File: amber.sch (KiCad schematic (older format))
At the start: 41 parts, among them J1 MJ-4PP-9

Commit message: Use a mid-mount TRRS jack SJ 43504
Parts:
- removed J1: MJ-4PP-9, kbd:MJ-4PP-9, symbol kbd:MJ-4PP-9
- added J?: SJ-43504-SMT-TR, amber:CUI_SJ-43504-SMT-TR-dual, symbol SJ-43504-SMT-TR:SJ-43504-SMT-TR
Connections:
- no-connect marks 5 -> 7
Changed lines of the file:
@@
 	8000 2100 8000 1800
-$Comp
-L kbd:MJ-4PP-9 J1
-U 1 1 60243402
-P 9400 4575
-F 0 "J1" H 9431 4851 50  0000 C CNN
-F 1 "MJ-4PP-9" H 9431 4760 50  0000 C CNN
-F 2 "kbd:MJ-4PP-9" H 9675 4750 50  0001 C CNN
-F 3 "~" H 9675 4750 50  0001 C CNN
-	1    9400 4575
-	1    0    0    -1
-$EndComp
 $Comp
 L power:GND #PWR05
 U 1 1 60243D5F
-P 9825 4725
-F 0 "#PWR05" H 9825 4475 50  0001 C CNN
-F 1 "GND" H 9830 4552 50  0000 C CNN
-F 2 "" H 9825 4725 50  0001 C CNN
-F 3 "" H 9825 4725 50  0001 C CNN
-	1    9825 4725
+P 9250 4675
+F 0 "#PWR05" H 9250 4425 50  0001 C CNN
+F 1 "GND" H 9255 4502 50  0000 C CNN
+F 2 "" H 9250 4675 50  0001 C CNN
+F 3 "" H 9250 4675 50  0001 C CNN
+	1    9250 4675
 	1    0    0    -1
 $EndComp
 Wire Wire Line
-	9600 4600 9825 4600
+	9025 4550 9250 4550
 Wire Wire Line
-	9825 4600 9825 4725
+	9250 4550 9250 4675
 $Comp
 L power:VCC #PWR04
 U 1 1 60246E67
-P 9825 4400
-F 0 "#PWR04" H 9825 4250 50  0001 C CNN
-F 1 "VCC" H 9840 4573 50  0000 C CNN
-F 2 "" H 9825 4400 50  0001 C CNN
-F 3 "" H 9825 4400 50  0001 C CNN
-	1    9825 4400
+P 9250 4300
+F 0 "#PWR04" H 9250 4150 50  0001 C CNN
+F 1 "VCC" H 9265 4473 50  0000 C CNN
+F 2 "" H 9250 4300 50  0001 C CNN
+F 3 "" H 9250 4300 50  0001 C CNN
+	1    9250 4300
 	1    0    0    -1
 $EndComp
 Wire Wire Line
-	9600 4550 9825 4550
+	9025 4450 9250 4450
 Wire Wire Line
-	9825 4550 9825 4400
-Text GLabel 9975 4650 2    50   Input ~ 0
+	9250 4450 9250 4300
+Text GLabel 9400 4850 2    50   Input ~ 0
 Serial
 Wire Wire Line
-	9600 4650 9975 4650
+	9025 4850 9400 4850
 Text GLabel 9750 2600 2    50   Input ~ 0
 Serial
@@
 NoConn ~ 9750 1900
 NoConn ~ 7875 2650
-NoConn ~ 9600 4500
+NoConn ~ 9025 4650
+$Comp
+L SJ-43504-SMT-TR:SJ-43504-SMT-TR J?
+U 1 1 6045EB21
+P 8825 4550
+F 0 "J?" H 8769 4931 50  0000 C CNN
+F 1 "SJ-43504-SMT-TR" H 8769 4840 50  0000 C CNN
+F 2 "amber:CUI_SJ-43504-SMT-TR-dual" H 8825 4550 50  0001 L BNN
+F 3 "" H 8825 4550 50  0001 L BNN
+F 4 "SJ-43504-SMT-TR" H 8825 4550 50  0001 L BNN "MP"
+F 5 "$0.83 USD" H 8825 4550 50  0001 L BNN "PRICE"
+F 6 "CUIINC" H 8825 4550 50  0001 L BNN "MF"
+F 7 "Good" H 8825 4550 50  0001 L BNN "AVAILABILITY"
+F 8 "None" H 8825 4550 50  0001 L BNN "PACKAGE"
+	1    8825 4550
+	1    0    0    -1
+$EndComp
+NoConn ~ 9025 4350
+NoConn ~ 9025 4750
 $EndSCHEMATC

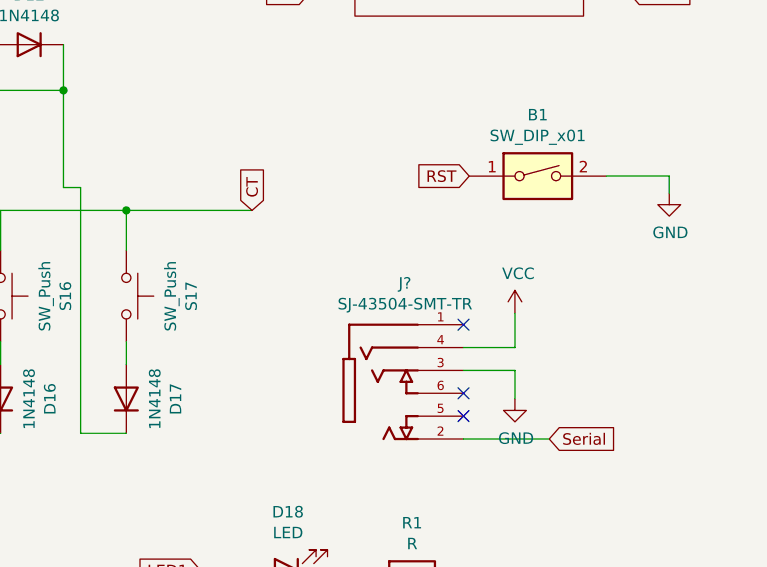
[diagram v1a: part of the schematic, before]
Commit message: Widen the promicro pad holes
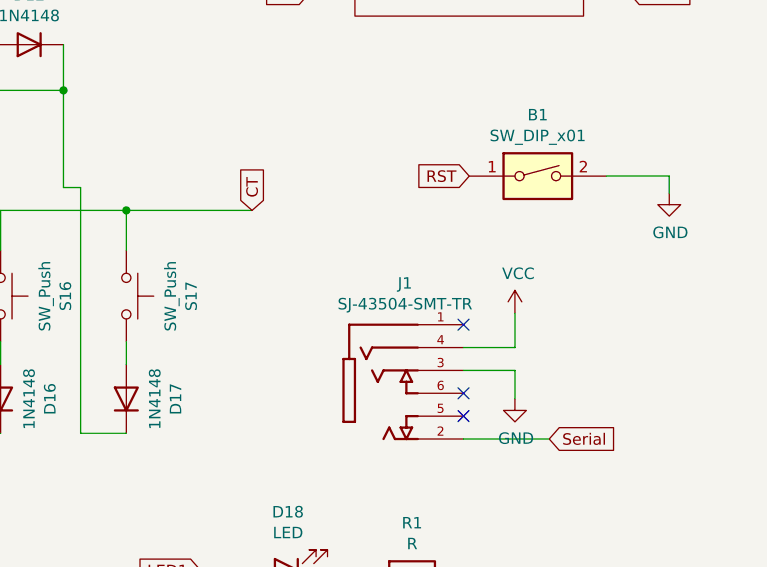
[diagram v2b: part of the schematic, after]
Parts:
- gave numbers to parts that had none: 1
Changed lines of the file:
@@
 NoConn ~ 9025 4650
 $Comp
-L SJ-43504-SMT-TR:SJ-43504-SMT-TR J?
+L SJ-43504-SMT-TR:SJ-43504-SMT-TR J1
 U 1 1 6045EB21
 P 8825 4550
-F 0 "J?" H 8769 4931 50  0000 C CNN
+F 0 "J1" H 8769 4931 50  0000 C CNN
 F 1 "SJ-43504-SMT-TR" H 8769 4840 50  0000 C CNN
 F 2 "amber:CUI_SJ-43504-SMT-TR-dual" H 8825 4550 50  0001 L BNN

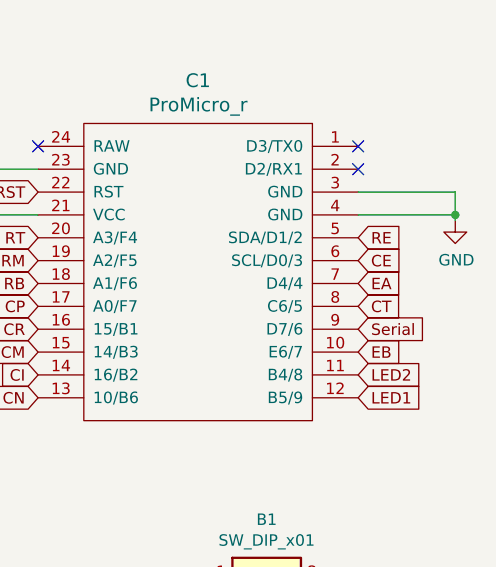
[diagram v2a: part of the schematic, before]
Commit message: Move serial to D1
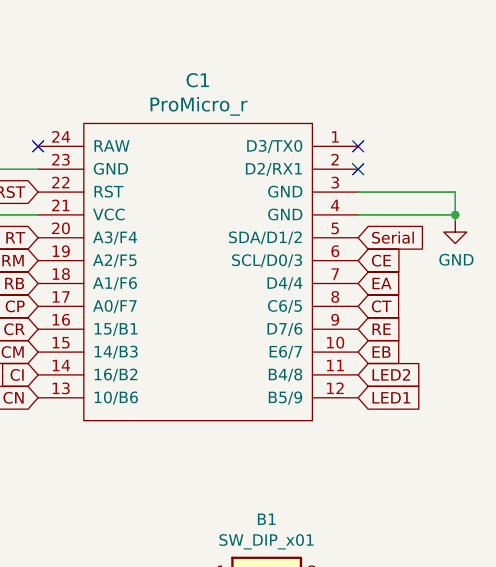
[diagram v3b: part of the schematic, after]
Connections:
- net RE: now also C1.9 (D7/6); no longer C1.5 (SDA/D1/2)
- net Serial: now also C1.5 (SDA/D1/2); no longer C1.9 (D7/6)
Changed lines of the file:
@@
 Wire Wire Line
 	9025 4850 9400 4850
-Text GLabel 9750 2600 2    50   Input ~ 0
+Text GLabel 9750 2200 2    50   Input ~ 0
 Serial
 $Comp
@@
 Text GLabel 9750 2300 2    50   Input ~ 0
 CE
-Text GLabel 9750 2200 2    50   Input ~ 0
+Text GLabel 9750 2600 2    50   Input ~ 0
 RE
 Wire Wire Line

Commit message: Add magnets, use side switch for reset
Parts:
- B1: footprint kbd:ResetSW -> amber:SW_SPST_EVQP7C
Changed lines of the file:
@@
 F 0 "B1" H 9350 3967 50  0000 C CNN
 F 1 "SW_DIP_x01" H 9350 3876 50  0000 C CNN
-F 2 "kbd:ResetSW" H 9350 3700 50  0001 C CNN
+F 2 "amber:SW_SPST_EVQP7C" H 9350 3700 50  0001 C CNN
 F 3 "~" H 9350 3700 50  0001 C CNN
 	1    9350 3700

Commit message: Update silkscreen
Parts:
- S1, S10, S11, S12, S13, S14, S16, S17, S2, S3, S4, S5, S6, S7, S8, S9: footprint kbd:CherryMX_MidHeight_Hotswap -> amber:CherryMX_MidHeight_Hotswap
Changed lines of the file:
@@
 F 0 "S1" H 2375 3410 50  0000 C CNN
 F 1 "SW_Push" H 2375 3319 50  0000 C CNN
-F 2 "kbd:CherryMX_MidHeight_Hotswap" H 2375 3325 50  0001 C CNN
+F 2 "amber:CherryMX_MidHeight_Hotswap" H 2375 3325 50  0001 C CNN
 F 3 "~" H 2375 3325 50  0001 C CNN
 	1    2375 3125
@@
 F 0 "S2" H 2375 2860 50  0000 C CNN
 F 1 "SW_Push" H 2375 2769 50  0000 C CNN
-F 2 "kbd:CherryMX_MidHeight_Hotswap" H 2375 2775 50  0001 C CNN
+F 2 "amber:CherryMX_MidHeight_Hotswap" H 2375 2775 50  0001 C CNN
 F 3 "~" H 2375 2775 50  0001 C CNN
 	1    2375 2575
@@
 F 0 "S3" H 3450 3410 50  0000 C CNN
 F 1 "SW_Push" H 3450 3319 50  0000 C CNN
-F 2 "kbd:CherryMX_MidHeight_Hotswap" H 3450 3325 50  0001 C CNN
+F 2 "amber:CherryMX_MidHeight_Hotswap" H 3450 3325 50  0001 C CNN
 F 3 "~" H 3450 3325 50  0001 C CNN
 	1    3450 3125
@@
 F 0 "S4" H 3450 2860 50  0000 C CNN
 F 1 "SW_Push" H 3450 2769 50  0000 C CNN
-F 2 "kbd:CherryMX_MidHeight_Hotswap" H 3450 2775 50  0001 C CNN
+F 2 "amber:CherryMX_MidHeight_Hotswap" H 3450 2775 50  0001 C CNN
 F 3 "~" H 3450 2775 50  0001 C CNN
 	1    3450 2575
@@
 F 0 "S6" H 4525 3410 50  0000 C CNN
 F 1 "SW_Push" H 4525 3319 50  0000 C CNN
-F 2 "kbd:CherryMX_MidHeight_Hotswap" H 4525 3325 50  0001 C CNN
+F 2 "amber:CherryMX_MidHeight_Hotswap" H 4525 3325 50  0001 C CNN
 F 3 "~" H 4525 3325 50  0001 C CNN
 	1    4525 3125
@@
 F 0 "S7" H 4525 2860 50  0000 C CNN
 F 1 "SW_Push" H 4525 2769 50  0000 C CNN
-F 2 "kbd:CherryMX_MidHeight_Hotswap" H 4525 2775 50  0001 C CNN
+F 2 "amber:CherryMX_MidHeight_Hotswap" H 4525 2775 50  0001 C CNN
 F 3 "~" H 4525 2775 50  0001 C CNN
 	1    4525 2575
@@
 F 0 "S8" H 4525 2310 50  0000 C CNN
 F 1 "SW_Push" H 4525 2219 50  0000 C CNN
-F 2 "kbd:CherryMX_MidHeight_Hotswap" H 4525 2225 50  0001 C CNN
+F 2 "amber:CherryMX_MidHeight_Hotswap" H 4525 2225 50  0001 C CNN
 F 3 "~" H 4525 2225 50  0001 C CNN
 	1    4525 2025
@@
 F 0 "S9" H 5600 3410 50  0000 C CNN
 F 1 "SW_Push" H 5600 3319 50  0000 C CNN
-F 2 "kbd:CherryMX_MidHeight_Hotswap" H 5600 3325 50  0001 C CNN
+F 2 "amber:CherryMX_MidHeight_Hotswap" H 5600 3325 50  0001 C CNN
 F 3 "~" H 5600 3325 50  0001 C CNN
 	1    5600 3125
@@
 F 0 "S10" H 5600 2860 50  0000 C CNN
 F 1 "SW_Push" H 5600 2769 50  0000 C CNN
-F 2 "kbd:CherryMX_MidHeight_Hotswap" H 5600 2775 50  0001 C CNN
+F 2 "amber:CherryMX_MidHeight_Hotswap" H 5600 2775 50  0001 C CNN
 F 3 "~" H 5600 2775 50  0001 C CNN
 	1    5600 2575
@@
 F 0 "S11" H 5600 2310 50  0000 C CNN
 F 1 "SW_Push" H 5600 2219 50  0000 C CNN
-F 2 "kbd:CherryMX_MidHeight_Hotswap" H 5600 2225 50  0001 C CNN
+F 2 "amber:CherryMX_MidHeight_Hotswap" H 5600 2225 50  0001 C CNN
 F 3 "~" H 5600 2225 50  0001 C CNN
 	1    5600 2025
@@
 F 0 "S12" H 6675 3410 50  0000 C CNN
 F 1 "SW_Push" H 6675 3319 50  0000 C CNN
-F 2 "kbd:CherryMX_MidHeight_Hotswap" H 6675 3325 50  0001 C CNN
+F 2 "amber:CherryMX_MidHeight_Hotswap" H 6675 3325 50  0001 C CNN
 F 3 "~" H 6675 3325 50  0001 C CNN
 	1    6675 3125
@@
 F 0 "S13" H 6675 2860 50  0000 C CNN
 F 1 "SW_Push" H 6675 2769 50  0000 C CNN
-F 2 "kbd:CherryMX_MidHeight_Hotswap" H 6675 2775 50  0001 C CNN
+F 2 "amber:CherryMX_MidHeight_Hotswap" H 6675 2775 50  0001 C CNN
 F 3 "~" H 6675 2775 50  0001 C CNN
 	1    6675 2575
@@
 F 0 "S14" H 6675 2310 50  0000 C CNN
 F 1 "SW_Push" H 6675 2219 50  0000 C CNN
-F 2 "kbd:CherryMX_MidHeight_Hotswap" H 6675 2225 50  0001 C CNN
+F 2 "amber:CherryMX_MidHeight_Hotswap" H 6675 2225 50  0001 C CNN
 F 3 "~" H 6675 2225 50  0001 C CNN
 	1    6675 2025
@@
 F 0 "S5" H 3450 2310 50  0000 C CNN
 F 1 "SW_Push" H 3450 2219 50  0000 C CNN
-F 2 "kbd:CherryMX_MidHeight_Hotswap" H 3450 2225 50  0001 C CNN
+F 2 "amber:CherryMX_MidHeight_Hotswap" H 3450 2225 50  0001 C CNN
 F 3 "~" H 3450 2225 50  0001 C CNN
 	1    3450 2025
@@
 F 0 "S16" H 7000 4510 50  0000 C CNN
 F 1 "SW_Push" H 7000 4419 50  0000 C CNN
-F 2 "kbd:CherryMX_MidHeight_Hotswap" H 7000 4425 50  0001 C CNN
+F 2 "amber:CherryMX_MidHeight_Hotswap" H 7000 4425 50  0001 C CNN
 F 3 "~" H 7000 4425 50  0001 C CNN
 	1    7000 4225
@@
 F 0 "S17" H 7550 4510 50  0000 C CNN
 F 1 "SW_Push" H 7550 4419 50  0000 C CNN
-F 2 "kbd:CherryMX_MidHeight_Hotswap" H 7550 4425 50  0001 C CNN
+F 2 "amber:CherryMX_MidHeight_Hotswap" H 7550 4425 50  0001 C CNN
 F 3 "~" H 7550 4425 50  0001 C CNN
 	1    7550 4225

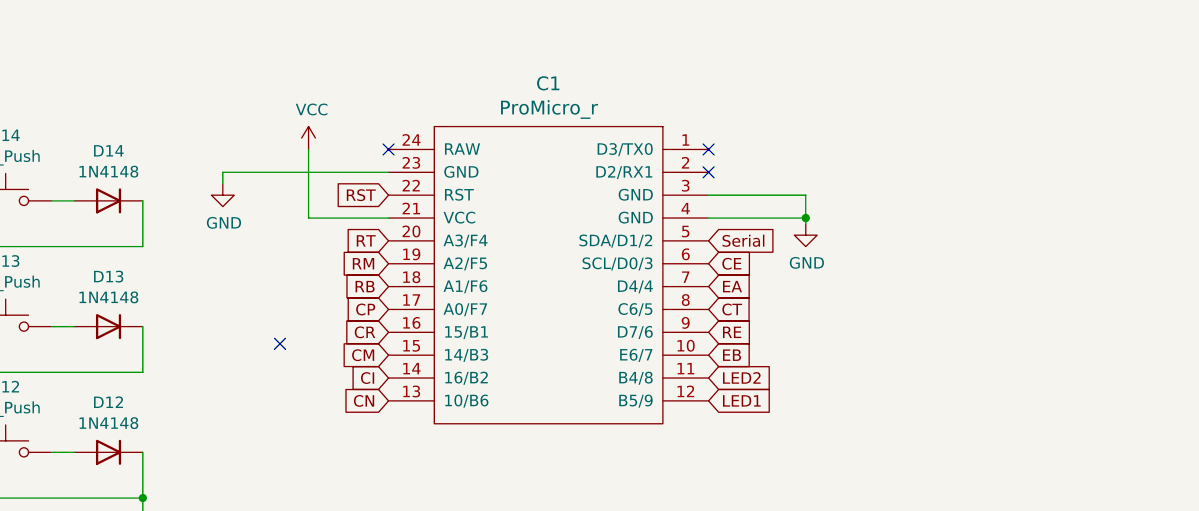
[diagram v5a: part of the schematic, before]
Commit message: Make a reversible MCU socket using jumpers
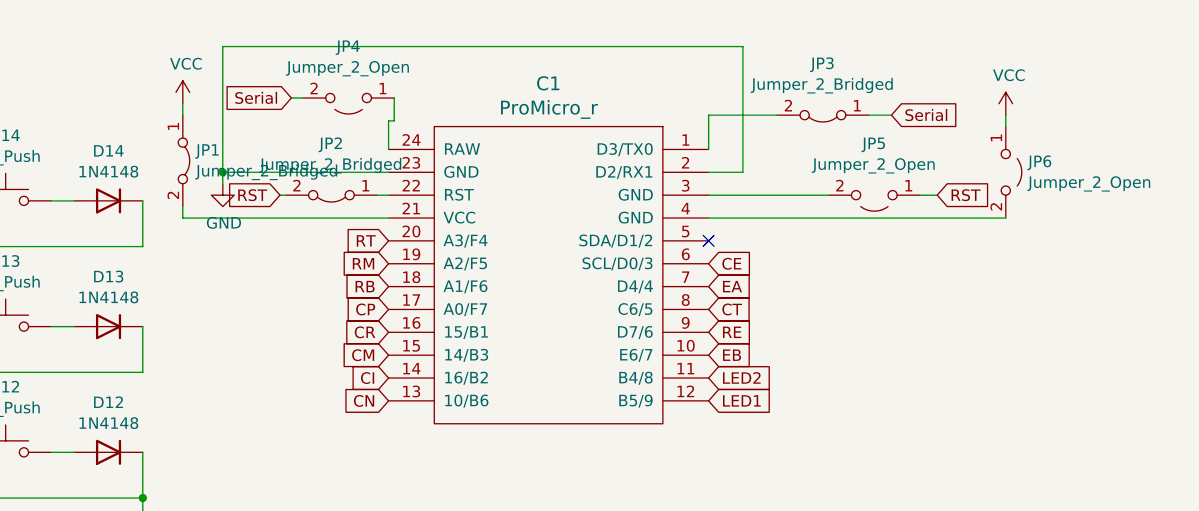
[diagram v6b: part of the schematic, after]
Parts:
- added JP1, JP2, JP3: Jumper_2_Bridged, Jumper:SolderJumper-2_P1.3mm_Bridged_Pad1.0x1.5mm, symbol Jumper:Jumper_2_Bridged
- added JP4, JP5, JP6: Jumper_2_Open, Jumper:SolderJumper-2_P1.3mm_Open_Pad1.0x1.5mm, symbol Jumper:Jumper_2_Open
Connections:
- net GND: now also C1.2 (D2/RX1); no longer C1.3 (GND), C1.4 (GND)
- net RST: now also JP2.2 (B), JP5.1 (A); no longer C1.22 (RST)
- net Serial: now also JP3.1 (A), JP4.2 (B); no longer C1.5 (SDA/D1/2)
- net VCC: now also JP1.1 (A), JP6.1 (A); no longer C1.21 (VCC)
- net at C1.1 (D3/TX0): now also JP3.2 (B)
- net at C1.24 (RAW): now also JP4.1 (A)
- new net: C1.21 (VCC), JP1.2 (B)
- new net: C1.22 (RST), JP2.1 (A)
- new net: C1.3 (GND), JP5.2 (B)
- new net: C1.4 (GND), JP6.2 (B)
- no-connect marks 7 -> 4
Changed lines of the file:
@@
 	1    0    0    -1
 $EndComp
-Text GLabel 8350 2000 0    50   Input ~ 0
+Text GLabel 7875 2000 0    50   Input ~ 0
 RST
 Text GLabel 9050 3700 0    50   Input ~ 0
@@
 L power:VCC #PWR03
 U 1 1 6023FBA7
-P 8000 1800
-F 0 "#PWR03" H 8000 1650 50  0001 C CNN
-F 1 "VCC" H 8015 1973 50  0000 C CNN
-F 2 "" H 8000 1800 50  0001 C CNN
-F 3 "" H 8000 1800 50  0001 C CNN
-	1    8000 1800
-	1    0    0    -1
-$EndComp
-Wire Wire Line
-	8350 2100 8000 2100
-Wire Wire Line
-	8000 2100 8000 1800
+P 11050 1650
+F 0 "#PWR03" H 11050 1500 50  0001 C CNN
+F 1 "VCC" H 11065 1823 50  0000 C CNN
+F 2 "" H 11050 1650 50  0001 C CNN
+F 3 "" H 11050 1650 50  0001 C CNN
+	1    11050 1650
+	1    0    0    -1
+$EndComp
 $Comp
 L power:GND #PWR05
@@
 Wire Wire Line
 	9025 4850 9400 4850
-Text GLabel 9750 2200 2    50   Input ~ 0
+Text GLabel 10550 1650 2    50   Input ~ 0
 Serial
 $Comp
@@
 Wire Wire Line
 	6450 4025 6450 3925
-$Comp
-L power:GND #PWR0101
-U 1 1 602E2507
-P 10175 2125
-F 0 "#PWR0101" H 10175 1875 50  0001 C CNN
-F 1 "GND" H 10180 1952 50  0000 C CNN
-F 2 "" H 10175 2125 50  0001 C CNN
-F 3 "" H 10175 2125 50  0001 C CNN
-	1    10175 2125
-	1    0    0    -1
-$EndComp
-Wire Wire Line
-	9750 2100 10175 2100
-Wire Wire Line
-	10175 2100 10175 2125
-Wire Wire Line
-	9750 2000 10175 2000
-Wire Wire Line
-	10175 2000 10175 2100
-Connection ~ 10175 2100
-NoConn ~ 8350 1800
-NoConn ~ 9750 1800
-NoConn ~ 9750 1900
-NoConn ~ 7875 2650
+NoConn ~ 9750 2200
 NoConn ~ 9025 4650
 $Comp
@@
 NoConn ~ 9025 4350
 NoConn ~ 9025 4750
+$Comp
+L Jumper:Jumper_2_Bridged JP1
+U 1 1 6058CB5A
+P 7450 1850
+F 0 "JP1" V 7404 1908 50  0000 L CNN
+F 1 "Jumper_2_Bridged" V 7495 1908 50  0000 L CNN
+F 2 "Jumper:SolderJumper-2_P1.3mm_Bridged_Pad1.0x1.5mm" H 7450 1850 50  0001 C CNN
+F 3 "~" H 7450 1850 50  0001 C CNN
+	1    7450 1850
+	0    1    1    0
+$EndComp
+Wire Wire Line
+	9750 1900 9900 1900
+Wire Wire Line
+	9900 1900 9900 1350
+Wire Wire Line
+	9900 1350 7625 1350
+Wire Wire Line
+	7625 1350 7625 1900
+Connection ~ 7625 1900
+Wire Wire Line
+	7450 2100 7450 2050
+Wire Wire Line
+	7450 2100 8350 2100
+Wire Wire Line
+	11050 1700 11050 1650
+$Comp
+L Jumper:Jumper_2_Open JP6
+U 1 1 6059F1AB
+P 11050 1900
+F 0 "JP6" V 11004 1998 50  0000 L CNN
+F 1 "Jumper_2_Open" V 11095 1998 50  0000 L CNN
+F 2 "Jumper:SolderJumper-2_P1.3mm_Open_Pad1.0x1.5mm" H 11050 1900 50  0001 C CNN
+F 3 "~" H 11050 1900 50  0001 C CNN
+	1    11050 1900
+	0    1    1    0
+$EndComp
+$Comp
+L power:VCC #PWR0101
+U 1 1 605A68A1
+P 7450 1600
+F 0 "#PWR0101" H 7450 1450 50  0001 C CNN
+F 1 "VCC" H 7465 1773 50  0000 C CNN
+F 2 "" H 7450 1600 50  0001 C CNN
+F 3 "" H 7450 1600 50  0001 C CNN
+	1    7450 1600
+	1    0    0    -1
+$EndComp
+Wire Wire Line
+	7450 1650 7450 1600
+$Comp
+L Jumper:Jumper_2_Bridged JP2
+U 1 1 605AB58C
+P 8100 2000
+F 0 "JP2" H 8100 1775 50  0000 C CNN
+F 1 "Jumper_2_Bridged" H 8100 1866 50  0000 C CNN
+F 2 "Jumper:SolderJumper-2_P1.3mm_Bridged_Pad1.0x1.5mm" H 8100 2000 50  0001 C CNN
+F 3 "~" H 8100 2000 50  0001 C CNN
+	1    8100 2000
+	-1   0    0    1
+$EndComp
+Wire Wire Line
+	8300 2000 8350 2000
+Wire Wire Line
+	7900 2000 7875 2000
+Text GLabel 10750 2000 2    50   Input ~ 0
+RST
+$Comp
+L Jumper:Jumper_2_Open JP5
+U 1 1 605B9572
+P 10475 2000
+F 0 "JP5" H 10475 1775 50  0000 C CNN
+F 1 "Jumper_2_Open" H 10475 1866 50  0000 C CNN
+F 2 "Jumper:SolderJumper-2_P1.3mm_Open_Pad1.0x1.5mm" H 10475 2000 50  0001 C CNN
+F 3 "~" H 10475 2000 50  0001 C CNN
+	1    10475 2000
+	-1   0    0    1
+$EndComp
+Wire Wire Line
+	9750 2000 10275 2000
+Wire Wire Line
+	10675 2000 10750 2000
+Wire Wire Line
+	9750 2100 11050 2100
+$Comp
+L Jumper:Jumper_2_Bridged JP3
+U 1 1 605DDE38
+P 10250 1650
+F 0 "JP3" H 10250 1425 50  0000 C CNN
+F 1 "Jumper_2_Bridged" H 10250 1516 50  0000 C CNN
+F 2 "Jumper:SolderJumper-2_P1.3mm_Bridged_Pad1.0x1.5mm" H 10250 1650 50  0001 C CNN
+F 3 "~" H 10250 1650 50  0001 C CNN
+	1    10250 1650
+	-1   0    0    1
+$EndComp
+Wire Wire Line
+	10550 1650 10450 1650
+Wire Wire Line
+	10050 1650 9750 1650
+Wire Wire Line
+	9750 1650 9750 1800
+Text GLabel 7925 1575 0    50   Input ~ 0
+Serial
+$Comp
+L Jumper:Jumper_2_Open JP4
+U 1 1 605E6466
+P 8175 1575
+F 0 "JP4" H 8175 1350 50  0000 C CNN
+F 1 "Jumper_2_Open" H 8175 1441 50  0000 C CNN
+F 2 "Jumper:SolderJumper-2_P1.3mm_Open_Pad1.0x1.5mm" H 8175 1575 50  0001 C CNN
+F 3 "~" H 8175 1575 50  0001 C CNN
+	1    8175 1575
+	-1   0    0    1
+$EndComp
+Wire Wire Line
+	7925 1575 7975 1575
+Wire Wire Line
+	8375 1575 8375 1675
+Wire Wire Line
+	8375 1675 8350 1675
+Wire Wire Line
+	8350 1675 8350 1800
 $EndSCHEMATC

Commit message: Fix the encoder/switch footprint
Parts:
- removed D15: 1N4148, amber:Diode_THT7.6_SOD123, symbol Diode:1N4148
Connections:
- net RE: now also S15.S2
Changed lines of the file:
@@
 	1    0    0    -1
-$EndComp
-$Comp
-L Diode:1N4148 D15
-U 1 1 601F9003
-P 6450 4675
-F 0 "D15" H 6450 4458 50  0000 C CNN
-F 1 "1N4148" H 6450 4549 50  0000 C CNN
-F 2 "amber:Diode_THT7.6_SOD123" H 6450 4500 50  0001 C CNN
-F 3 "https://assets.nexperia.com/documents/data-sheet/1N4148_1N4448.pdf" H 6450 4675 50  0001 C CNN
-	1    6450 4675
-	0    -1   -1   0
 $EndComp
 Wire Wire Line
 	6450 4425 6450 4525
-Wire Wire Line
-	6450 4825 6250 4825
 $Comp
 L Switch:SW_Push S16
@@
 Text GLabel 6450 3925 1    50   Input ~ 0
 CE
-Text GLabel 6250 4825 0    50   Input ~ 0
+Text GLabel 6450 4525 3    50   Input ~ 0
 RE
 Text GLabel 9750 2300 2    50   Input ~ 0
